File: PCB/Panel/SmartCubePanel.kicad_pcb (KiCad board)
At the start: 2 copper layers, 174.6 x 142.8 mm, 912 parts, among them J1 PogoPinPad, J1 SWD_Programmer, J1 Shield_Connector_Top_Left, J2 Conn_01x06, J2 Shield_Connector_Bottom_Left, J2 Shield_Connector_Top_Right, J3 PogoPinPad, J3 Shield_Connector_Bottom_Right, J3 Shield_Connector_Top_Right, J4 PogoPinPad, J4 Shield_Connector_Bottom_Right, J4 Shield_Connector_Top_Left, J5 Shield_Connector_Bottom_Left, U1 HallLinearSensor, U1 PY32F002BF15P6TU, U1 PogoPin, U2 PinHeaderTop, U2 PogoPin, U3 PinHeaderRight, U3 PogoPin, U4 PinHeaderBottom, U5 PinHeaderLeft

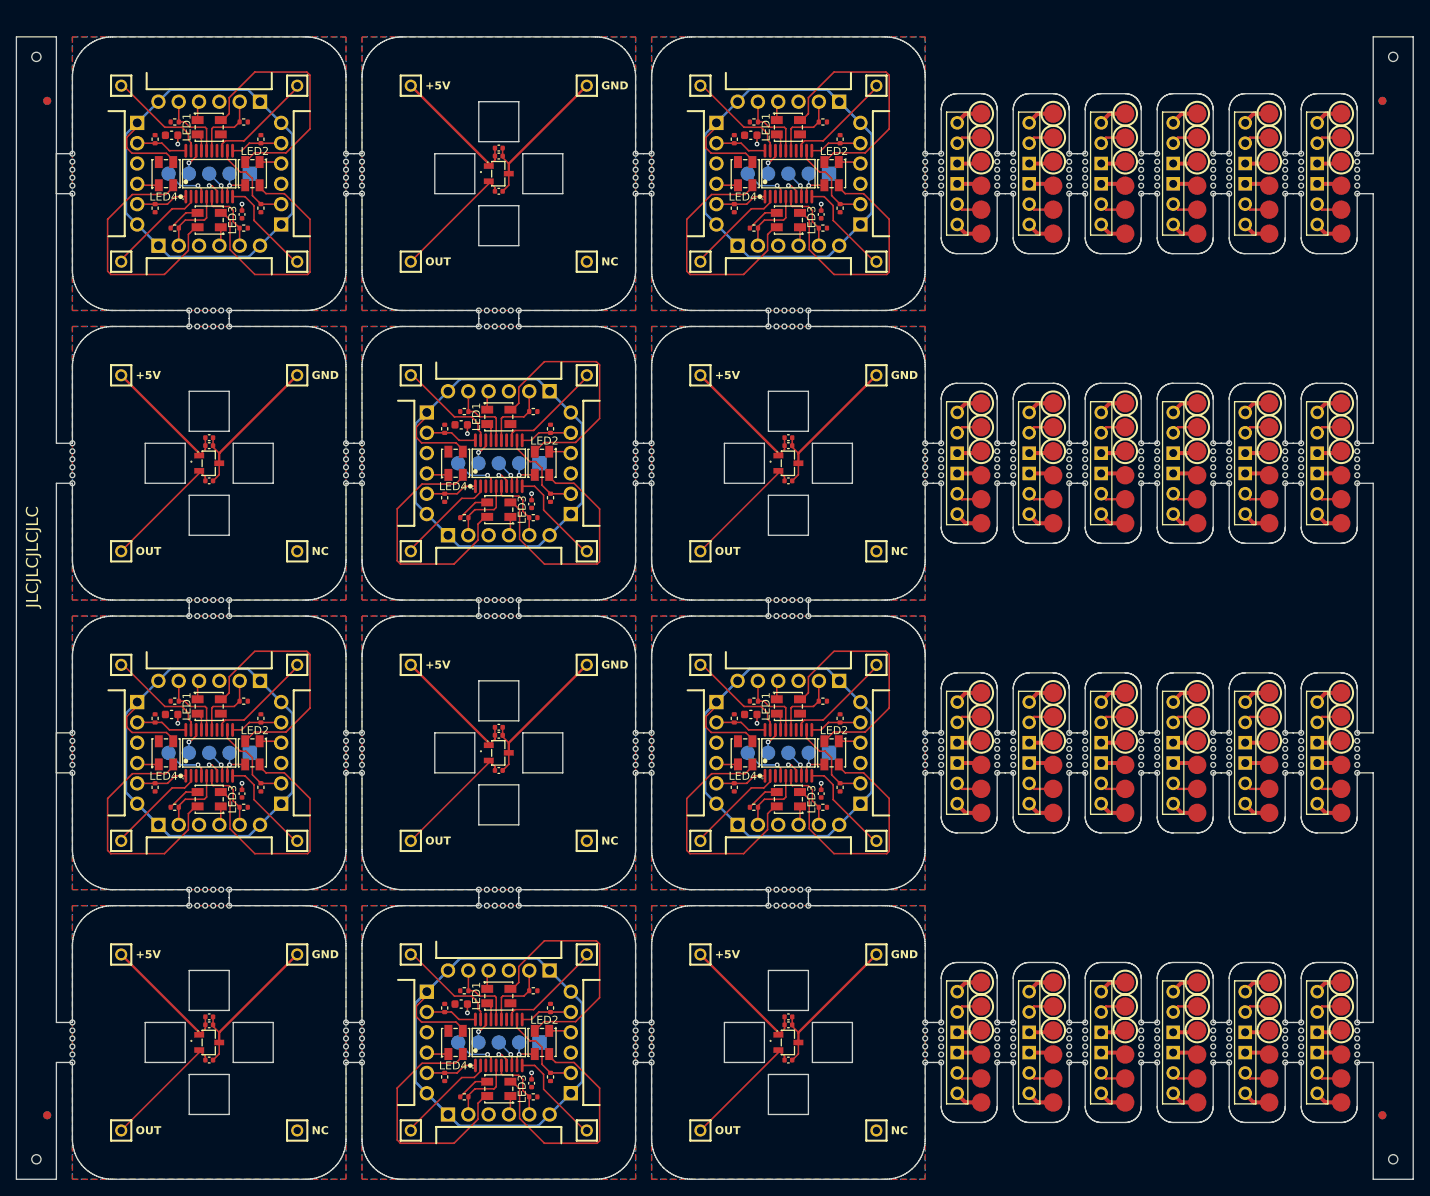
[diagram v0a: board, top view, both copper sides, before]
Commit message: Fix 3d model paths
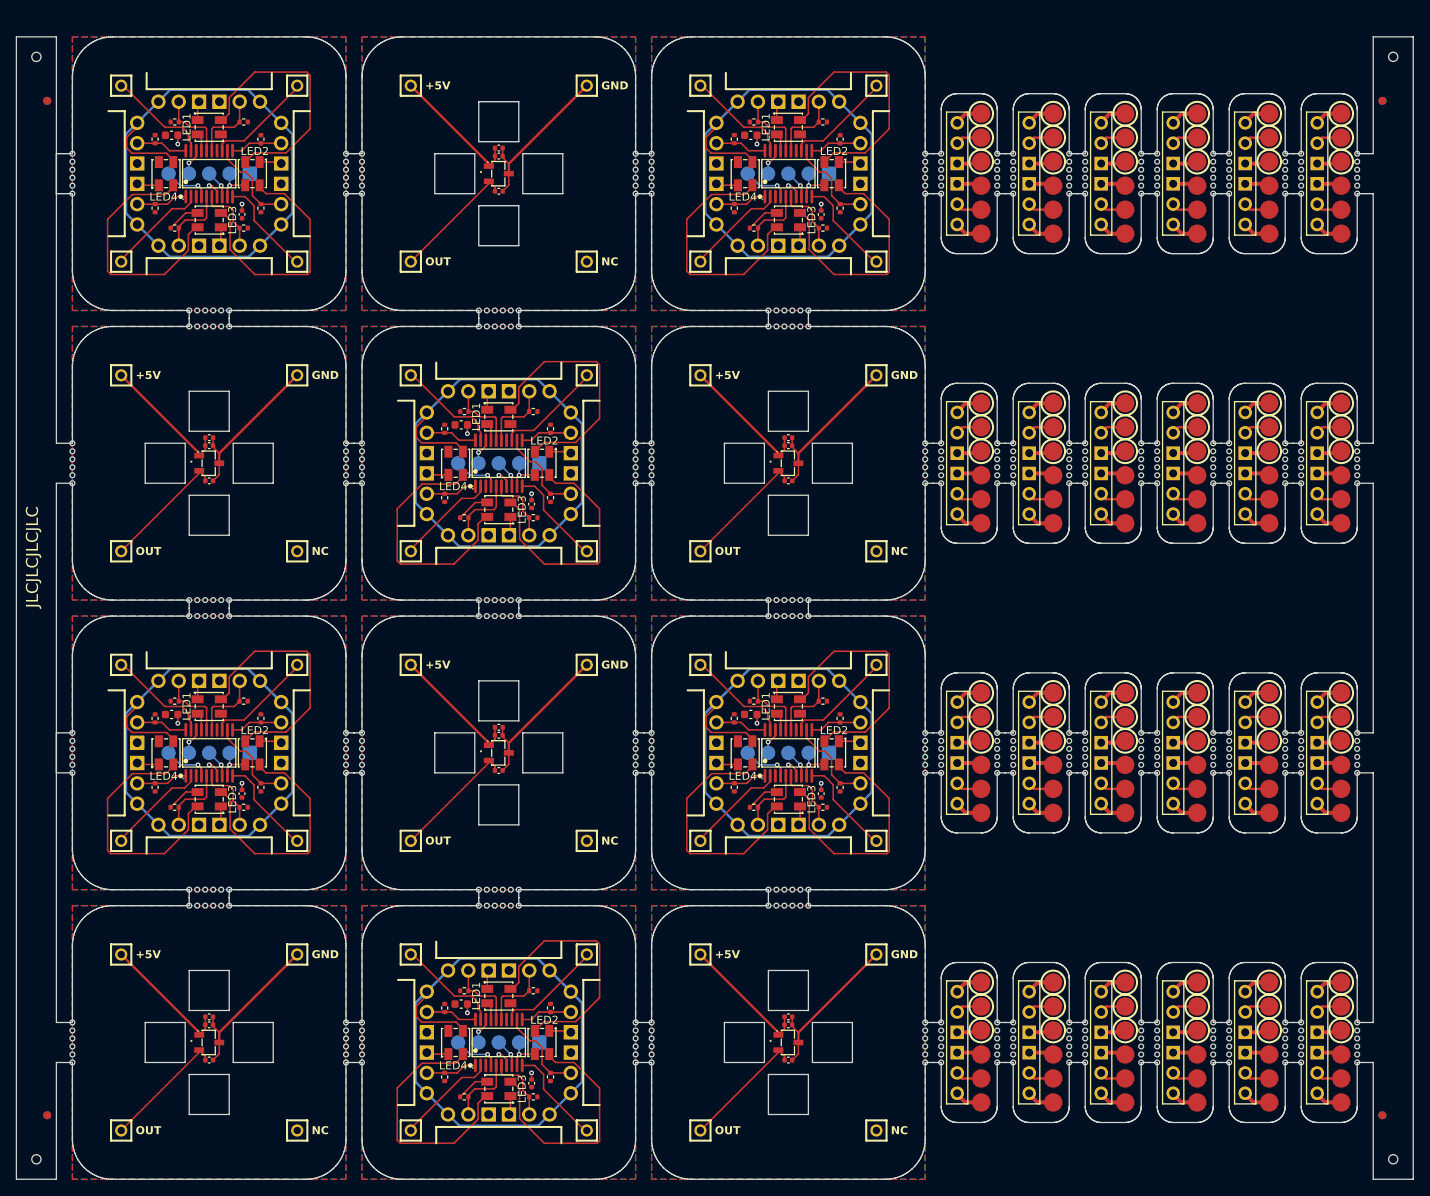
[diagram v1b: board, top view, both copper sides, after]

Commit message: Add power supply (wip) and update panel
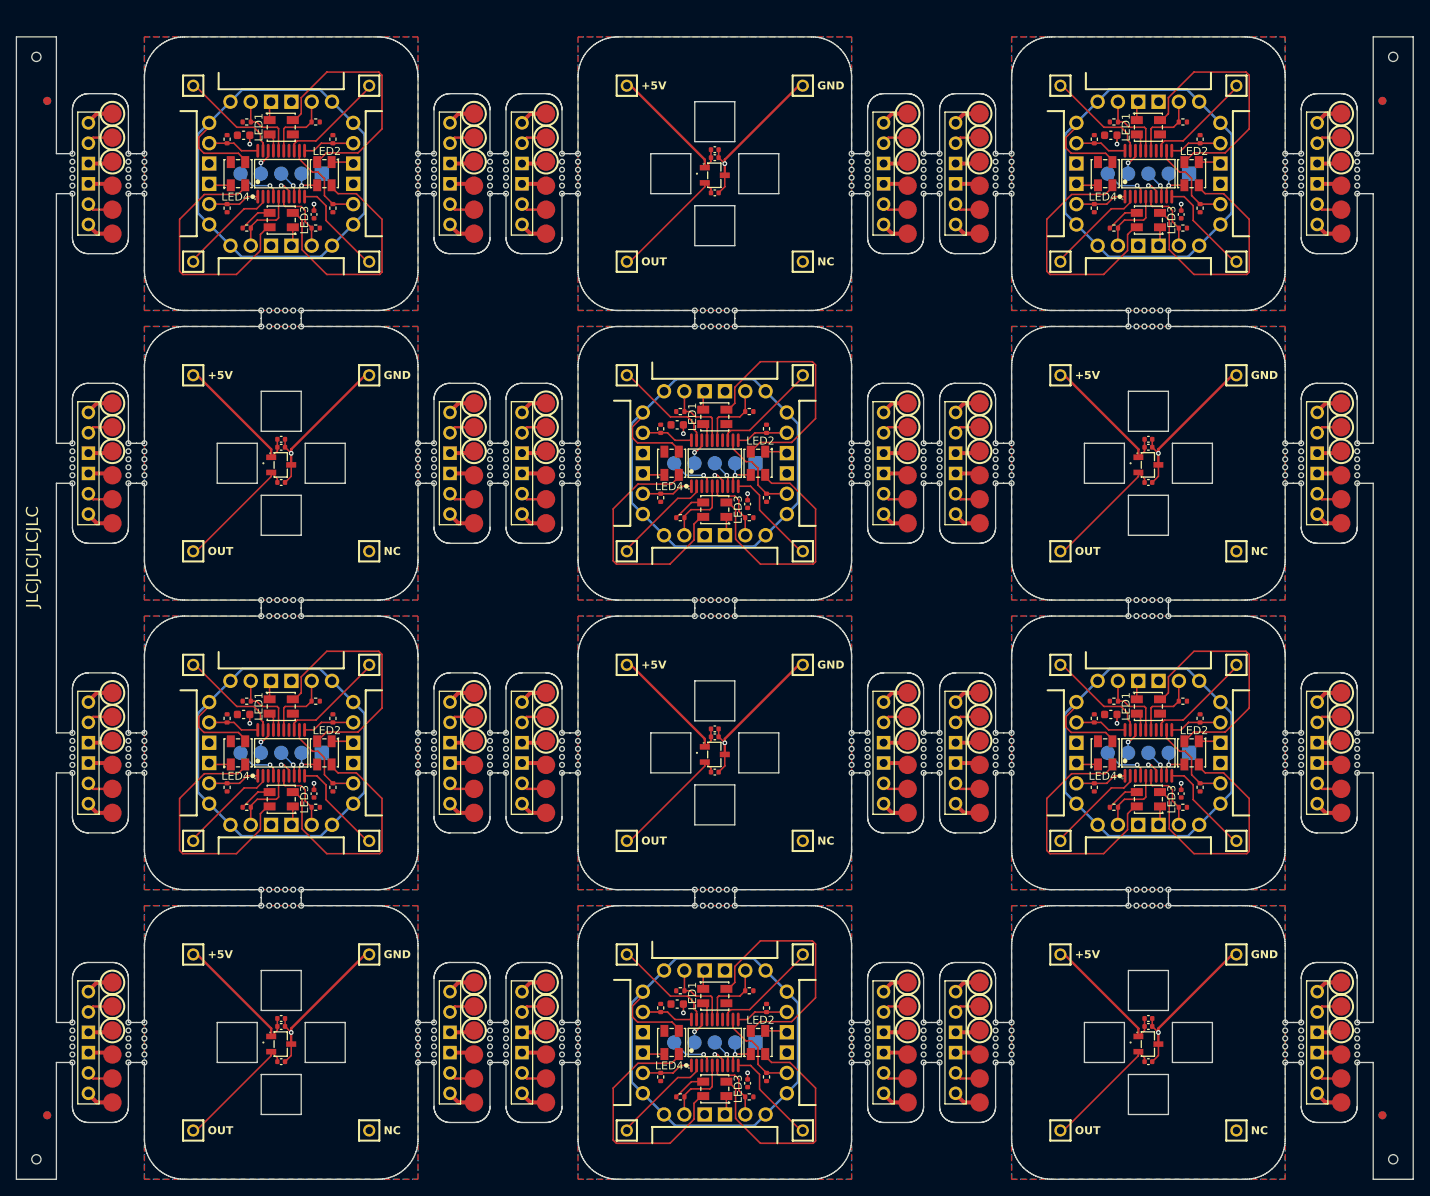
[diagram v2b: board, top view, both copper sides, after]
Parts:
- removed the C1 at (116.8, 68.5)
- removed the C1 at (153.0, 104.7)
- removed the C1 at (157.7, 147.9)
- removed the C1 at (85.3, 147.9)
- removed the C1 at (80.6, 32.3)
- removed the C1 at (153.0, 32.3)
- removed the C1 at (116.8, 140.9)
- removed the C1 at (85.3, 75.5)
- removed the C1 at (121.5, 111.7)
- removed the C1 at (157.7, 75.5)
- removed the C1 at (80.6, 104.7)
- removed the C1 at (121.5, 39.3)
- removed the C2 at (157.7, 70.1)
- removed the C2 at (85.3, 70.1)
- removed the C2 at (161.8, 114.6)
- removed the C2 at (161.8, 42.2)
- removed the C2 at (125.6, 78.4)
- removed the C2 at (89.4, 114.6)
- removed the C2 at (85.3, 142.5)
- removed the C2 at (125.6, 150.8)
- removed the C2 at (157.7, 142.5)
- removed the C2 at (121.5, 106.3)
- removed the C2 at (89.4, 42.2)
- removed the C2 at (121.5, 33.9)
- removed the C3 at (121.5, 34.9)
- removed the C3 at (85.3, 143.5)
- removed the C3 at (157.7, 143.5)
- removed the C3 at (157.7, 71.1)
- removed the C3 at (121.5, 107.3)
- removed the C3 at (85.3, 71.1)
- removed the J1 at (217.8, 38.6)
- removed the J1 at (217.8, 74.8)
- removed the J1 at (226.8, 147.2)
- removed the J1 at (181.8, 111.0)
- removed the J1 at (181.8, 74.8)
- removed the J1 at (217.8, 147.2)
- removed the J1 at (190.8, 111.0)
- removed the J1 at (199.8, 74.8)
- removed the J1 at (110.5, 26.1)
- removed the J1 at (181.8, 38.6)
- removed the J1 at (190.8, 38.6)
- removed the J1 at (146.7, 62.3)
- removed the J1 at (226.8, 74.8)
- removed the J1 at (217.8, 111.0)
- removed the J1 at (181.8, 147.2)
- removed the J1 at (146.7, 134.7)
- removed the J1 at (208.8, 111.0)
- removed the J1 at (208.8, 38.6)
- removed the J1 at (226.8, 38.6)
- removed the J1 at (74.3, 62.3)
- removed the J1 at (226.8, 111.0)
- removed the J1 at (208.8, 147.2)
- removed the J1 at (74.3, 134.7)
- removed the J1 at (199.8, 147.2)
- removed the J1 at (85.4, 109.5)
- removed the J1 at (157.8, 109.5)
- removed the J1 at (121.6, 73.3)
- removed the J1 at (157.8, 37.1)
- removed the J1 at (85.4, 37.1)
- removed the J1 at (121.6, 145.7)
- removed the J1 at (110.5, 98.5)
- removed the J1 at (190.8, 74.8)
- removed the J1 at (199.8, 38.6)
- removed the J1 at (190.8, 147.2)
- removed the J1 at (208.8, 74.8)
- removed the J1 at (199.8, 111.0)
- removed the J2 at (205.8, 37.1)
- removed the J2 at (132.5, 134.7)
- removed the J2 at (132.5, 62.3)
- removed the J2 at (74.3, 84.3)
- removed the J2 at (187.8, 145.7)
- removed the J2 at (205.8, 73.3)
- removed the J2 at (178.8, 145.7)
- removed the J2 at (110.5, 120.5)
- removed the J2 at (187.8, 37.1)
- removed the J2 at (214.8, 145.7)
- removed the J2 at (146.7, 156.7)
- removed the J2 at (110.5, 48.1)
- removed the J2 at (223.8, 37.1)
- removed the J2 at (196.8, 37.1)
- removed the J2 at (187.8, 109.5)
- removed the J2 at (178.8, 109.5)
- removed the J2 at (168.7, 26.1)
- removed the J2 at (146.7, 84.3)
- removed the J2 at (223.8, 73.3)
- removed the J2 at (214.8, 109.5)
- removed the J2 at (205.8, 109.5)
- removed the J2 at (178.8, 73.3)
- removed the J2 at (74.3, 156.7)
- removed the J2 at (96.3, 26.1)
- removed the J2 at (214.8, 37.1)
- removed the J2 at (187.8, 73.3)
- removed the J2 at (96.3, 98.5)
- removed the J2 at (223.8, 145.7)
- removed the J2 at (214.8, 73.3)
- removed the J2 at (196.8, 109.5)
- removed the J2 at (178.8, 37.1)
- removed the J2 at (168.7, 98.5)
- removed the J2 at (196.8, 73.3)
- removed the J2 at (205.8, 145.7)
- removed the J2 at (196.8, 145.7)
- removed the J2 at (223.8, 109.5)
- removed the J3 at (132.5, 26.1)
- removed the J3 at (208.8, 77.8)
- removed the J3 at (132.5, 84.3)
- removed the J3 at (208.8, 114.0)
- removed the J3 at (199.8, 150.2)
- removed the J3 at (132.5, 156.7)
- removed the J3 at (132.5, 98.5)
- removed the J3 at (96.3, 134.7)
- removed the J3 at (217.8, 150.2)
- removed the J3 at (226.8, 77.8)
- removed the J3 at (199.8, 114.0)
- removed the J3 at (190.8, 114.0)
- removed the J3 at (168.7, 62.3)
- removed the J3 at (226.8, 114.0)
- removed the J3 at (96.3, 62.3)
- removed the J3 at (181.8, 150.2)
- removed the J3 at (181.8, 77.8)
- removed the J3 at (199.8, 41.6)
- removed the J3 at (190.8, 77.8)
- removed the J3 at (96.3, 48.1)
- removed the J3 at (217.8, 41.6)
- removed the J3 at (168.7, 134.7)
- removed the J3 at (217.8, 77.8)
- removed the J3 at (181.8, 41.6)
- removed the J3 at (208.8, 150.2)
- removed the J3 at (190.8, 41.6)
- removed the J3 at (226.8, 150.2)
- removed the J3 at (168.7, 48.1)
- removed the J3 at (168.7, 120.5)
- removed the J3 at (96.3, 120.5)
- removed the J3 at (181.8, 114.0)
- removed the J3 at (208.8, 41.6)
- removed the J3 at (226.8, 41.6)
- removed the J3 at (217.8, 114.0)
- removed the J3 at (199.8, 77.8)
- removed the J3 at (190.8, 150.2)
- removed the J4 at (208.8, 117.0)
- removed the J4 at (146.7, 26.1)
- removed the J4 at (181.8, 44.6)
- removed the J4 at (168.7, 156.7)
- removed the J4 at (181.8, 117.0)
- removed the J4 at (217.8, 153.2)
- removed the J4 at (190.8, 80.8)
- removed the J4 at (132.5, 120.5)
- removed the J4 at (208.8, 44.6)
- removed the J4 at (208.8, 153.2)
- removed the J4 at (96.3, 84.3)
- removed the J4 at (74.3, 98.5)
- removed the J4 at (226.8, 117.0)
- removed the J4 at (181.8, 153.2)
- removed the J4 at (132.5, 48.1)
- removed the J4 at (217.8, 44.6)
- removed the J4 at (226.8, 80.8)
- removed the J4 at (199.8, 44.6)
- removed the J4 at (74.3, 26.1)
- removed the J4 at (199.8, 117.0)
- removed the J4 at (199.8, 153.2)
- removed the J4 at (110.5, 134.7)
- removed the J4 at (226.8, 44.6)
- removed the J4 at (168.7, 84.3)
- removed the J4 at (208.8, 80.8)
- removed the J4 at (226.8, 153.2)
- removed the J4 at (190.8, 44.6)
- removed the J4 at (181.8, 80.8)
- removed the J4 at (190.8, 117.0)
- removed the J4 at (190.8, 153.2)
- removed the J4 at (217.8, 117.0)
- removed the J4 at (96.3, 156.7)
- removed the J4 at (110.5, 62.3)
- removed the J4 at (199.8, 80.8)
- removed the J4 at (217.8, 80.8)
- removed the J4 at (146.7, 98.5)
- removed the J5 at (146.7, 48.1)
- removed the J5 at (74.3, 48.1)
- removed the J5 at (110.5, 156.7)
- removed the J5 at (74.3, 120.5)
- removed the J5 at (146.7, 120.5)
- removed the J5 at (110.5, 84.3)
- removed the LED1 at (157.7, 103.7)
- removed the LED1 at (121.5, 67.5)
- removed the LED1 at (85.3, 31.3)
- removed the LED1 at (85.3, 103.7)
- removed the LED1 at (157.7, 31.3)
- removed the LED1 at (121.5, 139.9)
- removed the LED2 at (163.1, 109.5)
- removed the LED2 at (163.1, 37.1)
- removed the LED2 at (126.9, 73.3)
- removed the LED2 at (90.7, 109.5)
- removed the LED2 at (90.7, 37.1)
- removed the LED2 at (126.9, 145.7)
- removed the LED3 at (85.3, 115.3)
- removed the LED3 at (85.3, 42.9)
- removed the LED3 at (157.7, 42.9)
- removed the LED3 at (157.7, 115.3)
- removed the LED3 at (121.5, 79.1)
- removed the LED3 at (121.5, 151.5)
- removed the LED4 at (116.1, 73.3)
- removed the LED4 at (79.9, 109.5)
- removed the LED4 at (152.3, 37.1)
- removed the LED4 at (116.1, 145.7)
- removed the LED4 at (152.3, 109.5)
- removed the LED4 at (79.9, 37.1)
- removed the R1 at (117.2, 66.8)
- removed the R1 at (117.2, 139.2)
- removed the R1 at (153.4, 30.6)
- removed the R1 at (81.0, 103.0)
- removed the R1 at (81.0, 30.6)
- removed the R1 at (153.4, 103.0)
- removed the R2 at (89.6, 103.0)
- removed the R2 at (125.8, 66.8)
- removed the R2 at (162.0, 103.0)
- removed the R2 at (125.8, 139.2)
- removed the R2 at (89.6, 30.6)
- removed the R2 at (162.0, 30.6)
- removed the R3 at (91.8, 105.2)
- removed the R3 at (164.2, 32.8)
- removed the R3 at (128.0, 141.4)
- removed the R3 at (128.0, 69.0)
- removed the R3 at (164.2, 105.2)
- removed the R3 at (91.8, 32.8)
- removed the R4 at (164.2, 113.8)
- removed the R4 at (91.8, 41.4)
- removed the R4 at (128.0, 77.6)
- removed the R4 at (91.8, 113.8)
- removed the R4 at (128.0, 150.0)
- removed the R4 at (164.2, 41.4)
- removed the R5 at (125.8, 152.5)
- removed the R5 at (125.8, 80.1)
- removed the R5 at (89.6, 43.9)
- removed the R5 at (162.0, 43.9)
- removed the R5 at (89.6, 116.3)
- removed the R5 at (162.0, 116.3)
- removed the R6 at (81.0, 116.3)
- removed the R6 at (117.2, 152.5)
- removed the R6 at (153.4, 43.9)
- removed the R6 at (153.4, 116.3)
- removed the R6 at (81.0, 43.9)
- removed the R6 at (117.2, 80.1)
- removed the R7 at (78.5, 113.8)
- removed the R7 at (78.5, 41.4)
- removed the R7 at (150.9, 113.8)
- removed the R7 at (150.9, 41.4)
- removed the R7 at (114.7, 150.0)
- removed the R7 at (114.7, 77.6)
- removed the R8 at (114.7, 141.4)
- removed the R8 at (78.5, 105.2)
- removed the R8 at (114.7, 69.0)
- removed the R8 at (78.5, 32.8)
- removed the R8 at (150.9, 105.2)
- removed the R8 at (150.9, 32.8)
- removed the U1 at (181.8, 102.0)
- removed the U1 at (190.8, 65.8)
- removed the U1 at (226.8, 102.0)
- removed the U1 at (226.8, 65.8)
- removed the U1 at (181.8, 29.6)
- removed the U1 at (121.5, 37.1)
- removed the U1 at (190.8, 29.6)
- removed the U1 at (190.8, 102.0)
- removed the U1 at (121.5, 109.5)
- removed the U1 at (199.8, 65.8)
- removed the U1 at (157.7, 145.7)
- removed the U1 at (208.8, 138.2)
- removed the U1 at (217.8, 138.2)
- removed the U1 at (121.5, 73.3)
- removed the U1 at (121.5, 145.7)
- removed the U1 at (157.7, 109.5)
- removed the U1 at (181.8, 65.8)
- removed the U1 at (157.7, 37.1)
- removed the U1 at (85.3, 73.3)
- removed the U1 at (208.8, 29.6)
- removed the U1 at (217.8, 29.6)
- removed the U1 at (199.8, 29.6)
- removed the U1 at (208.8, 102.0)
- removed the U1 at (190.8, 138.2)
- removed the U1 at (85.3, 37.1)
- removed the U1 at (85.3, 109.5)
- removed the U1 at (199.8, 138.2)
- removed the U1 at (181.8, 138.2)
- removed the U1 at (199.8, 102.0)
- removed the U1 at (217.8, 102.0)
- removed the U1 at (157.7, 73.3)
- removed the U1 at (208.8, 65.8)
- removed the U1 at (85.3, 145.7)
- removed the U1 at (226.8, 138.2)
- removed the U1 at (217.8, 65.8)
- removed the U1 at (226.8, 29.6)
- removed the U2 at (181.8, 141.2)
- removed the U2 at (190.8, 105.0)
- removed the U2 at (190.8, 141.2)
- removed the U2 at (226.8, 68.8)
- removed the U2 at (181.8, 32.6)
- removed the U2 at (217.8, 105.0)
- removed the U2 at (157.7, 28.1)
- removed the U2 at (199.8, 68.8)
- removed the U2 at (217.8, 141.2)
- removed the U2 at (190.8, 68.8)
- removed the U2 at (199.8, 141.2)
- removed the U2 at (226.8, 105.0)
- removed the U2 at (226.8, 141.2)
- removed the U2 at (121.5, 136.7)
- removed the U2 at (85.3, 28.1)
- removed the U2 at (157.7, 100.5)
- removed the U2 at (121.5, 64.3)
- removed the U2 at (208.8, 32.6)
- removed the U2 at (226.8, 32.6)
- removed the U2 at (181.8, 105.0)
- removed the U2 at (208.8, 141.2)
- removed the U2 at (217.8, 32.6)
- removed the U2 at (181.8, 68.8)
- removed the U2 at (199.8, 105.0)
- removed the U2 at (199.8, 32.6)
- removed the U2 at (208.8, 105.0)
- removed the U2 at (85.3, 100.5)
- removed the U2 at (190.8, 32.6)
- removed the U2 at (217.8, 68.8)
- removed the U2 at (208.8, 68.8)
- removed the U3 at (208.8, 71.8)
- removed the U3 at (199.8, 144.2)
- removed the U3 at (199.8, 71.8)
- removed the U3 at (226.8, 108.0)
- removed the U3 at (226.8, 35.6)
- removed the U3 at (166.7, 109.5)
- removed the U3 at (190.8, 71.8)
- removed the U3 at (217.8, 108.0)
- removed the U3 at (208.8, 144.2)
- removed the U3 at (181.8, 71.8)
- removed the U3 at (199.8, 35.6)
- removed the U3 at (94.3, 37.1)
- removed the U3 at (217.8, 35.6)
- removed the U3 at (217.8, 71.8)
- removed the U3 at (190.8, 144.2)
- removed the U3 at (181.8, 144.2)
- removed the U3 at (181.8, 108.0)
- removed the U3 at (208.8, 108.0)
- removed the U3 at (226.8, 144.2)
- removed the U3 at (181.8, 35.6)
- removed the U3 at (190.8, 108.0)
- removed the U3 at (217.8, 144.2)
- removed the U3 at (94.3, 109.5)
- removed the U3 at (130.5, 73.3)
- removed the U3 at (190.8, 35.6)
- removed the U3 at (130.5, 145.7)
- removed the U3 at (199.8, 108.0)
- removed the U3 at (208.8, 35.6)
- removed the U3 at (226.8, 71.8)
- removed the U3 at (166.7, 37.1)
- removed the U4 at (121.5, 154.7)
- removed the U4 at (85.3, 46.1)
- removed the U4 at (85.3, 118.5)
- removed the U4 at (157.7, 118.5)
- removed the U4 at (121.5, 82.3)
- removed the U4 at (157.7, 46.1)
- removed the U5 at (112.5, 145.7)
- removed the U5 at (148.7, 37.1)
- removed the U5 at (148.7, 109.5)
- removed the U5 at (76.3, 37.1)
- removed the U5 at (76.3, 109.5)
- removed the U5 at (112.5, 73.3)
- added C1: 10nF, Capacitor_SMD:C_0402_1005Metric, F.Cu at (94.3, 148.1)
- added C1: 10uF, Capacitor_SMD:C_0603_1608Metric, F.Cu at (198.0, 104.7)
- added C1: 10uF, Capacitor_SMD:C_0603_1608Metric, F.Cu at (89.6, 104.7)
- added C1: 10nF, Capacitor_SMD:C_0402_1005Metric, F.Cu at (202.7, 148.1)
- added C1: 10nF, Capacitor_SMD:C_0402_1005Metric, F.Cu at (94.3, 75.7)
- added C1: 10uF, Capacitor_SMD:C_0603_1608Metric, F.Cu at (143.8, 140.9)
- added C1: 10uF, Capacitor_SMD:C_0603_1608Metric, F.Cu at (143.8, 68.5)
- added C1: 10uF, Capacitor_SMD:C_0603_1608Metric, F.Cu at (89.6, 32.3)
- added C1: 10uF, Capacitor_SMD:C_0603_1608Metric, F.Cu at (198.0, 32.3)
- added C1: 10nF, Capacitor_SMD:C_0402_1005Metric, F.Cu at (148.5, 39.5)
- added C1: 10nF, Capacitor_SMD:C_0402_1005Metric, F.Cu at (148.5, 111.9)
- added C1: 10nF, Capacitor_SMD:C_0402_1005Metric, F.Cu at (202.7, 75.7)
- added C2: 1nF, Capacitor_SMD:C_0402_1005Metric, F.Cu at (202.7, 70.3)
- added C2: 1nF, Capacitor_SMD:C_0402_1005Metric, F.Cu at (94.3, 142.7)
- added C2: 100nF, Capacitor_SMD:C_0402_1005Metric, F.Cu at (206.8, 114.6)
- added C2: 100nF, Capacitor_SMD:C_0402_1005Metric, F.Cu at (98.4, 42.2)
- added C2: 1nF, Capacitor_SMD:C_0402_1005Metric, F.Cu at (148.5, 34.1)
- added C2: 1nF, Capacitor_SMD:C_0402_1005Metric, F.Cu at (202.7, 142.7)
- added C2: 100nF, Capacitor_SMD:C_0402_1005Metric, F.Cu at (152.6, 150.8)
- added C2: 100nF, Capacitor_SMD:C_0402_1005Metric, F.Cu at (206.8, 42.2)
- added C2: 1nF, Capacitor_SMD:C_0402_1005Metric, F.Cu at (94.3, 70.3)
- added C2: 1nF, Capacitor_SMD:C_0402_1005Metric, F.Cu at (148.5, 106.5)
- added C2: 100nF, Capacitor_SMD:C_0402_1005Metric, F.Cu at (98.4, 114.6)
- added C2: 100nF, Capacitor_SMD:C_0402_1005Metric, F.Cu at (152.6, 78.4)
- added C3: 1nF, Capacitor_SMD:C_0402_1005Metric, F.Cu at (148.5, 35.1)
- added C3: 1nF, Capacitor_SMD:C_0402_1005Metric, F.Cu at (202.7, 71.3)
- added C3: 1nF, Capacitor_SMD:C_0402_1005Metric, F.Cu at (202.7, 143.7)
- added C3: 1nF, Capacitor_SMD:C_0402_1005Metric, F.Cu at (94.3, 71.3)
- added C3: 1nF, Capacitor_SMD:C_0402_1005Metric, F.Cu at (94.3, 143.7)
- added C3: 1nF, Capacitor_SMD:C_0402_1005Metric, F.Cu at (148.5, 107.5)
- added J1: PogoPinPad, CustomFootprints:PogoPinPad, F.Cu at (118.4, 38.6)
- added J1: PogoPinPad, CustomFootprints:PogoPinPad, F.Cu at (181.6, 74.8)
- added J1: PogoPinPad, CustomFootprints:PogoPinPad, F.Cu at (181.6, 111.0)
- added J1: PogoPinPad, CustomFootprints:PogoPinPad, F.Cu at (73.2, 147.2)
- added J1: Shield_Connector_Top_Left, CustomFootprints:HDR-TH_1P-V-F-1, F.Cu at (83.3, 62.3)
- added J1: PogoPinPad, CustomFootprints:PogoPinPad, F.Cu at (118.4, 111.0)
- added J1: Shield_Connector_Top_Left, CustomFootprints:HDR-TH_1P-V-F-1, F.Cu at (83.3, 134.7)
- added J1: PogoPinPad, CustomFootprints:PogoPinPad, F.Cu at (226.8, 111.0)
- added J1: PogoPinPad, CustomFootprints:PogoPinPad, F.Cu at (172.6, 74.8)
- added J1: PogoPinPad, CustomFootprints:PogoPinPad, F.Cu at (226.8, 38.6)
- added J1: PogoPinPad, CustomFootprints:PogoPinPad, F.Cu at (73.2, 38.6)
- added J1: PogoPinPad, CustomFootprints:PogoPinPad, F.Cu at (181.6, 38.6)
- added J1: PogoPinPad, CustomFootprints:PogoPinPad, F.Cu at (172.6, 38.6)
- added J1: Shield_Connector_Top_Left, CustomFootprints:HDR-TH_1P-V-F-1, F.Cu at (137.5, 98.5)
- added J1: PogoPinPad, CustomFootprints:PogoPinPad, F.Cu at (172.6, 111.0)
- added J1: PogoPinPad, CustomFootprints:PogoPinPad, F.Cu at (127.4, 147.2)
- added J1: PogoPinPad, CustomFootprints:PogoPinPad, F.Cu at (73.2, 74.8)
- added J1: Shield_Connector_Top_Left, CustomFootprints:HDR-TH_1P-V-F-1, F.Cu at (191.7, 134.7)
- added J1: PogoPinPad, CustomFootprints:PogoPinPad, F.Cu at (118.4, 147.2)
- added J1: PogoPinPad, CustomFootprints:PogoPinPad, F.Cu at (73.2, 111.0)
- added J1: PogoPinPad, CustomFootprints:PogoPinPad, F.Cu at (127.4, 111.0)
- added J1: PogoPinPad, CustomFootprints:PogoPinPad, F.Cu at (226.8, 147.2)
- added J1: PogoPinPad, CustomFootprints:PogoPinPad, F.Cu at (226.8, 74.8)
- added J1: PogoPinPad, CustomFootprints:PogoPinPad, F.Cu at (118.4, 74.8)
- added J1: SWD_Programmer, CustomFootprints:SWD_Pad, B.Cu at (94.4, 109.5)
- added J1: SWD_Programmer, CustomFootprints:SWD_Pad, B.Cu at (94.4, 37.1)
- added J1: SWD_Programmer, CustomFootprints:SWD_Pad, B.Cu at (148.6, 145.7)
- added J1: SWD_Programmer, CustomFootprints:SWD_Pad, B.Cu at (202.8, 109.5)
- added J1: SWD_Programmer, CustomFootprints:SWD_Pad, B.Cu at (148.6, 73.3)
- added J1: SWD_Programmer, CustomFootprints:SWD_Pad, B.Cu at (202.8, 37.1)
- added J1: PogoPinPad, CustomFootprints:PogoPinPad, F.Cu at (127.4, 38.6)
- added J1: PogoPinPad, CustomFootprints:PogoPinPad, F.Cu at (127.4, 74.8)
- added J1: PogoPinPad, CustomFootprints:PogoPinPad, F.Cu at (172.6, 147.2)
- added J1: PogoPinPad, CustomFootprints:PogoPinPad, F.Cu at (181.6, 147.2)
- added J1: Shield_Connector_Top_Left, CustomFootprints:HDR-TH_1P-V-F-1, F.Cu at (191.7, 62.3)
- added J1: Shield_Connector_Top_Left, CustomFootprints:HDR-TH_1P-V-F-1, F.Cu at (137.5, 26.1)
- added J2: Conn_01x06, CustomFootprints:Connector_PinHeader_2.54mm_Vertical, F.Cu at (115.4, 73.3)
- added J2: Conn_01x06, CustomFootprints:Connector_PinHeader_2.54mm_Vertical, F.Cu at (115.4, 37.1)
- added J2: Conn_01x06, CustomFootprints:Connector_PinHeader_2.54mm_Vertical, F.Cu at (178.6, 73.3)
- added J2: Conn_01x06, CustomFootprints:Connector_PinHeader_2.54mm_Vertical, F.Cu at (70.2, 73.3)
- added J2: Conn_01x06, CustomFootprints:Connector_PinHeader_2.54mm_Vertical, F.Cu at (124.4, 73.3)
- added J2: Conn_01x06, CustomFootprints:Connector_PinHeader_2.54mm_Vertical, F.Cu at (70.2, 109.5)
- added J2: Conn_01x06, CustomFootprints:Connector_PinHeader_2.54mm_Vertical, F.Cu at (169.6, 109.5)
- added J2: Shield_Connector_Bottom_Left, CustomFootprints:HDR-TH_1P-V-F-1, F.Cu at (137.5, 120.5)
- added J2: Shield_Connector_Bottom_Left, CustomFootprints:HDR-TH_1P-V-F-1, F.Cu at (83.3, 156.7)
- added J2: Conn_01x06, CustomFootprints:Connector_PinHeader_2.54mm_Vertical, F.Cu at (169.6, 37.1)
- added J2: Conn_01x06, CustomFootprints:Connector_PinHeader_2.54mm_Vertical, F.Cu at (223.8, 37.1)
- added J2: Shield_Connector_Top_Right, CustomFootprints:HDR-TH_1P-V-F-1, F.Cu at (105.3, 98.5)
- added J2: Shield_Connector_Bottom_Left, CustomFootprints:HDR-TH_1P-V-F-1, F.Cu at (137.5, 48.1)
- added J2: Conn_01x06, CustomFootprints:Connector_PinHeader_2.54mm_Vertical, F.Cu at (178.6, 145.7)
- added J2: Conn_01x06, CustomFootprints:Connector_PinHeader_2.54mm_Vertical, F.Cu at (169.6, 73.3)
- added J2: Shield_Connector_Top_Right, CustomFootprints:HDR-TH_1P-V-F-1, F.Cu at (159.5, 134.7)
- added J2: Conn_01x06, CustomFootprints:Connector_PinHeader_2.54mm_Vertical, F.Cu at (115.4, 145.7)
- added J2: Conn_01x06, CustomFootprints:Connector_PinHeader_2.54mm_Vertical, F.Cu at (124.4, 109.5)
- added J2: Shield_Connector_Bottom_Left, CustomFootprints:HDR-TH_1P-V-F-1, F.Cu at (191.7, 84.3)
- added J2: Shield_Connector_Top_Right, CustomFootprints:HDR-TH_1P-V-F-1, F.Cu at (213.7, 98.5)
- added J2: Conn_01x06, CustomFootprints:Connector_PinHeader_2.54mm_Vertical, F.Cu at (223.8, 109.5)
- added J2: Conn_01x06, CustomFootprints:Connector_PinHeader_2.54mm_Vertical, F.Cu at (70.2, 37.1)
- added J2: Shield_Connector_Bottom_Left, CustomFootprints:HDR-TH_1P-V-F-1, F.Cu at (83.3, 84.3)
- added J2: Shield_Connector_Bottom_Left, CustomFootprints:HDR-TH_1P-V-F-1, F.Cu at (191.7, 156.7)
- added J2: Conn_01x06, CustomFootprints:Connector_PinHeader_2.54mm_Vertical, F.Cu at (124.4, 145.7)
- added J2: Shield_Connector_Top_Right, CustomFootprints:HDR-TH_1P-V-F-1, F.Cu at (159.5, 62.3)
- added J2: Shield_Connector_Top_Right, CustomFootprints:HDR-TH_1P-V-F-1, F.Cu at (105.3, 26.1)
- added J2: Conn_01x06, CustomFootprints:Connector_PinHeader_2.54mm_Vertical, F.Cu at (115.4, 109.5)
- added J2: Shield_Connector_Top_Right, CustomFootprints:HDR-TH_1P-V-F-1, F.Cu at (213.7, 26.1)
- added J2: Conn_01x06, CustomFootprints:Connector_PinHeader_2.54mm_Vertical, F.Cu at (124.4, 37.1)
- added J2: Conn_01x06, CustomFootprints:Connector_PinHeader_2.54mm_Vertical, F.Cu at (223.8, 145.7)
- added J2: Conn_01x06, CustomFootprints:Connector_PinHeader_2.54mm_Vertical, F.Cu at (178.6, 37.1)
- added J2: Conn_01x06, CustomFootprints:Connector_PinHeader_2.54mm_Vertical, F.Cu at (169.6, 145.7)
- added J2: Conn_01x06, CustomFootprints:Connector_PinHeader_2.54mm_Vertical, F.Cu at (178.6, 109.5)
- added J2: Conn_01x06, CustomFootprints:Connector_PinHeader_2.54mm_Vertical, F.Cu at (70.2, 145.7)
- added J2: Conn_01x06, CustomFootprints:Connector_PinHeader_2.54mm_Vertical, F.Cu at (223.8, 73.3)
- added J3: PogoPinPad, CustomFootprints:PogoPinPad, F.Cu at (181.6, 77.8)
- added J3: PogoPinPad, CustomFootprints:PogoPinPad, F.Cu at (226.8, 41.6)
- added J3: PogoPinPad, CustomFootprints:PogoPinPad, F.Cu at (181.6, 114.0)
- added J3: PogoPinPad, CustomFootprints:PogoPinPad, F.Cu at (127.4, 114.0)
- added J3: PogoPinPad, CustomFootprints:PogoPinPad, F.Cu at (226.8, 77.8)
- added J3: PogoPinPad, CustomFootprints:PogoPinPad, F.Cu at (118.4, 114.0)
- added J3: PogoPinPad, CustomFootprints:PogoPinPad, F.Cu at (118.4, 41.6)
- added J3: PogoPinPad, CustomFootprints:PogoPinPad, F.Cu at (226.8, 150.2)
- added J3: PogoPinPad, CustomFootprints:PogoPinPad, F.Cu at (127.4, 150.2)
- added J3: PogoPinPad, CustomFootprints:PogoPinPad, F.Cu at (172.6, 150.2)
- added J3: PogoPinPad, CustomFootprints:PogoPinPad, F.Cu at (73.2, 114.0)
- added J3: Shield_Connector_Bottom_Right, CustomFootprints:HDR-TH_1P-V-F-1, F.Cu at (105.3, 48.1)
- added J3: PogoPinPad, CustomFootprints:PogoPinPad, F.Cu at (181.6, 150.2)
- added J3: Shield_Connector_Bottom_Right, CustomFootprints:HDR-TH_1P-V-F-1, F.Cu at (159.5, 156.7)
- added J3: Shield_Connector_Top_Right, CustomFootprints:HDR-TH_1P-V-F-1, F.Cu at (159.5, 26.1)
- added J3: PogoPinPad, CustomFootprints:PogoPinPad, F.Cu at (172.6, 114.0)
- added J3: Shield_Connector_Top_Right, CustomFootprints:HDR-TH_1P-V-F-1, F.Cu at (105.3, 62.3)
- added J3: PogoPinPad, CustomFootprints:PogoPinPad, F.Cu at (172.6, 77.8)
- added J3: PogoPinPad, CustomFootprints:PogoPinPad, F.Cu at (73.2, 150.2)
- added J3: PogoPinPad, CustomFootprints:PogoPinPad, F.Cu at (181.6, 41.6)
- added J3: PogoPinPad, CustomFootprints:PogoPinPad, F.Cu at (73.2, 41.6)
- added J3: PogoPinPad, CustomFootprints:PogoPinPad, F.Cu at (226.8, 114.0)
- added J3: PogoPinPad, CustomFootprints:PogoPinPad, F.Cu at (118.4, 150.2)
- added J3: Shield_Connector_Top_Right, CustomFootprints:HDR-TH_1P-V-F-1, F.Cu at (105.3, 134.7)
- added J3: PogoPinPad, CustomFootprints:PogoPinPad, F.Cu at (127.4, 77.8)
- added J3: PogoPinPad, CustomFootprints:PogoPinPad, F.Cu at (118.4, 77.8)
- added J3: Shield_Connector_Top_Right, CustomFootprints:HDR-TH_1P-V-F-1, F.Cu at (213.7, 62.3)
- added J3: PogoPinPad, CustomFootprints:PogoPinPad, F.Cu at (73.2, 77.8)
- added J3: Shield_Connector_Bottom_Right, CustomFootprints:HDR-TH_1P-V-F-1, F.Cu at (105.3, 120.5)
- added J3: Shield_Connector_Bottom_Right, CustomFootprints:HDR-TH_1P-V-F-1, F.Cu at (159.5, 84.3)
- added J3: Shield_Connector_Top_Right, CustomFootprints:HDR-TH_1P-V-F-1, F.Cu at (213.7, 134.7)
- added J3: Shield_Connector_Bottom_Right, CustomFootprints:HDR-TH_1P-V-F-1, F.Cu at (213.7, 48.1)
- added J3: PogoPinPad, CustomFootprints:PogoPinPad, F.Cu at (172.6, 41.6)
- added J3: Shield_Connector_Top_Right, CustomFootprints:HDR-TH_1P-V-F-1, F.Cu at (159.5, 98.5)
- added J3: PogoPinPad, CustomFootprints:PogoPinPad, F.Cu at (127.4, 41.6)
- added J3: Shield_Connector_Bottom_Right, CustomFootprints:HDR-TH_1P-V-F-1, F.Cu at (213.7, 120.5)
- added J4: PogoPinPad, CustomFootprints:PogoPinPad, F.Cu at (73.2, 80.8)
- added J4: PogoPinPad, CustomFootprints:PogoPinPad, F.Cu at (226.8, 153.2)
- added J4: PogoPinPad, CustomFootprints:PogoPinPad, F.Cu at (172.6, 153.2)
- added J4: PogoPinPad, CustomFootprints:PogoPinPad, F.Cu at (226.8, 80.8)
- added J4: PogoPinPad, CustomFootprints:PogoPinPad, F.Cu at (73.2, 117.0)
- added J4: Shield_Connector_Top_Left, CustomFootprints:HDR-TH_1P-V-F-1, F.Cu at (83.3, 98.5)
- added J4: Shield_Connector_Bottom_Right, CustomFootprints:HDR-TH_1P-V-F-1, F.Cu at (159.5, 120.5)
- added J4: Shield_Connector_Top_Left, CustomFootprints:HDR-TH_1P-V-F-1, F.Cu at (137.5, 62.3)
- added J4: PogoPinPad, CustomFootprints:PogoPinPad, F.Cu at (127.4, 44.6)
- added J4: PogoPinPad, CustomFootprints:PogoPinPad, F.Cu at (118.4, 80.8)
- added J4: PogoPinPad, CustomFootprints:PogoPinPad, F.Cu at (181.6, 153.2)
- added J4: PogoPinPad, CustomFootprints:PogoPinPad, F.Cu at (172.6, 44.6)
- added J4: PogoPinPad, CustomFootprints:PogoPinPad, F.Cu at (118.4, 153.2)
- added J4: PogoPinPad, CustomFootprints:PogoPinPad, F.Cu at (172.6, 117.0)
- added J4: Shield_Connector_Top_Left, CustomFootprints:HDR-TH_1P-V-F-1, F.Cu at (83.3, 26.1)
- added J4: PogoPinPad, CustomFootprints:PogoPinPad, F.Cu at (226.8, 117.0)
- added J4: PogoPinPad, CustomFootprints:PogoPinPad, F.Cu at (181.6, 80.8)
- added J4: PogoPinPad, CustomFootprints:PogoPinPad, F.Cu at (73.2, 153.2)
- added J4: Shield_Connector_Bottom_Right, CustomFootprints:HDR-TH_1P-V-F-1, F.Cu at (105.3, 156.7)
- added J4: Shield_Connector_Top_Left, CustomFootprints:HDR-TH_1P-V-F-1, F.Cu at (191.7, 26.1)
- added J4: PogoPinPad, CustomFootprints:PogoPinPad, F.Cu at (181.6, 44.6)
- added J4: PogoPinPad, CustomFootprints:PogoPinPad, F.Cu at (73.2, 44.6)
- added J4: Shield_Connector_Bottom_Right, CustomFootprints:HDR-TH_1P-V-F-1, F.Cu at (213.7, 156.7)
- added J4: Shield_Connector_Top_Left, CustomFootprints:HDR-TH_1P-V-F-1, F.Cu at (191.7, 98.5)
- added J4: PogoPinPad, CustomFootprints:PogoPinPad, F.Cu at (127.4, 153.2)
- added J4: Shield_Connector_Top_Left, CustomFootprints:HDR-TH_1P-V-F-1, F.Cu at (137.5, 134.7)
- added J4: Shield_Connector_Bottom_Right, CustomFootprints:HDR-TH_1P-V-F-1, F.Cu at (213.7, 84.3)
- added J4: Shield_Connector_Bottom_Right, CustomFootprints:HDR-TH_1P-V-F-1, F.Cu at (159.5, 48.1)
- added J4: PogoPinPad, CustomFootprints:PogoPinPad, F.Cu at (118.4, 117.0)
- added J4: Shield_Connector_Bottom_Right, CustomFootprints:HDR-TH_1P-V-F-1, F.Cu at (105.3, 84.3)
- added J4: PogoPinPad, CustomFootprints:PogoPinPad, F.Cu at (172.6, 80.8)
- added J4: PogoPinPad, CustomFootprints:PogoPinPad, F.Cu at (127.4, 117.0)
- added J4: PogoPinPad, CustomFootprints:PogoPinPad, F.Cu at (118.4, 44.6)
- added J4: PogoPinPad, CustomFootprints:PogoPinPad, F.Cu at (226.8, 44.6)
- added J4: PogoPinPad, CustomFootprints:PogoPinPad, F.Cu at (181.6, 117.0)
- added J4: PogoPinPad, CustomFootprints:PogoPinPad, F.Cu at (127.4, 80.8)
- added J5: Shield_Connector_Bottom_Left, CustomFootprints:HDR-TH_1P-V-F-1, F.Cu at (83.3, 48.1)
- added J5: Shield_Connector_Bottom_Left, CustomFootprints:HDR-TH_1P-V-F-1, F.Cu at (83.3, 120.5)
- added J5: Shield_Connector_Bottom_Left, CustomFootprints:HDR-TH_1P-V-F-1, F.Cu at (191.7, 120.5)
- added J5: Shield_Connector_Bottom_Left, CustomFootprints:HDR-TH_1P-V-F-1, F.Cu at (137.5, 84.3)
- added J5: Shield_Connector_Bottom_Left, CustomFootprints:HDR-TH_1P-V-F-1, F.Cu at (137.5, 156.7)
- added J5: Shield_Connector_Bottom_Left, CustomFootprints:HDR-TH_1P-V-F-1, F.Cu at (191.7, 48.1)
- added LED1: SK6812MINI-HS, CustomFootprints:LED-SK6812MINI-HS, F.Cu at (94.3, 103.7)
- added LED1: SK6812MINI-HS, CustomFootprints:LED-SK6812MINI-HS, F.Cu at (148.5, 67.5)
- added LED1: SK6812MINI-HS, CustomFootprints:LED-SK6812MINI-HS, F.Cu at (148.5, 139.9)
- added LED1: SK6812MINI-HS, CustomFootprints:LED-SK6812MINI-HS, F.Cu at (202.7, 31.3)
- added LED1: SK6812MINI-HS, CustomFootprints:LED-SK6812MINI-HS, F.Cu at (94.3, 31.3)
- added LED1: SK6812MINI-HS, CustomFootprints:LED-SK6812MINI-HS, F.Cu at (202.7, 103.7)
- added LED2: SK6812MINI-HS, CustomFootprints:LED-SK6812MINI-HS, F.Cu at (208.1, 37.1)
- added LED2: SK6812MINI-HS, CustomFootprints:LED-SK6812MINI-HS, F.Cu at (153.9, 145.7)
- added LED2: SK6812MINI-HS, CustomFootprints:LED-SK6812MINI-HS, F.Cu at (99.7, 109.5)
- added LED2: SK6812MINI-HS, CustomFootprints:LED-SK6812MINI-HS, F.Cu at (153.9, 73.3)
- added LED2: SK6812MINI-HS, CustomFootprints:LED-SK6812MINI-HS, F.Cu at (208.1, 109.5)
- added LED2: SK6812MINI-HS, CustomFootprints:LED-SK6812MINI-HS, F.Cu at (99.7, 37.1)
- added LED3: SK6812MINI-HS, CustomFootprints:LED-SK6812MINI-HS, F.Cu at (94.3, 42.9)
- added LED3: SK6812MINI-HS, CustomFootprints:LED-SK6812MINI-HS, F.Cu at (202.7, 42.9)
- added LED3: SK6812MINI-HS, CustomFootprints:LED-SK6812MINI-HS, F.Cu at (202.7, 115.3)
- added LED3: SK6812MINI-HS, CustomFootprints:LED-SK6812MINI-HS, F.Cu at (148.5, 151.5)
- added LED3: SK6812MINI-HS, CustomFootprints:LED-SK6812MINI-HS, F.Cu at (148.5, 79.1)
- added LED3: SK6812MINI-HS, CustomFootprints:LED-SK6812MINI-HS, F.Cu at (94.3, 115.3)
- added LED4: SK6812MINI-HS, CustomFootprints:LED-SK6812MINI-HS, F.Cu at (197.3, 37.1)
- added LED4: SK6812MINI-HS, CustomFootprints:LED-SK6812MINI-HS, F.Cu at (197.3, 109.5)
- added LED4: SK6812MINI-HS, CustomFootprints:LED-SK6812MINI-HS, F.Cu at (88.9, 37.1)
- added LED4: SK6812MINI-HS, CustomFootprints:LED-SK6812MINI-HS, F.Cu at (143.1, 145.7)
- added LED4: SK6812MINI-HS, CustomFootprints:LED-SK6812MINI-HS, F.Cu at (88.9, 109.5)
- added LED4: SK6812MINI-HS, CustomFootprints:LED-SK6812MINI-HS, F.Cu at (143.1, 73.3)
- added R1: 10k, Resistor_SMD:R_0402_1005Metric, F.Cu at (198.4, 30.6)
- added R1: 10k, Resistor_SMD:R_0402_1005Metric, F.Cu at (144.2, 66.8)
- added R1: 10k, Resistor_SMD:R_0402_1005Metric, F.Cu at (198.4, 103.0)
- added R1: 10k, Resistor_SMD:R_0402_1005Metric, F.Cu at (144.2, 139.2)
- added R1: 10k, Resistor_SMD:R_0402_1005Metric, F.Cu at (90.0, 103.0)
- added R1: 10k, Resistor_SMD:R_0402_1005Metric, F.Cu at (90.0, 30.6)
- added R2: 10k, Resistor_SMD:R_0402_1005Metric, F.Cu at (207.0, 103.0)
- added R2: 10k, Resistor_SMD:R_0402_1005Metric, F.Cu at (152.8, 66.8)
- added R2: 10k, Resistor_SMD:R_0402_1005Metric, F.Cu at (207.0, 30.6)
- added R2: 10k, Resistor_SMD:R_0402_1005Metric, F.Cu at (98.6, 103.0)
- added R2: 10k, Resistor_SMD:R_0402_1005Metric, F.Cu at (98.6, 30.6)
- added R2: 10k, Resistor_SMD:R_0402_1005Metric, F.Cu at (152.8, 139.2)
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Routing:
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- added copper zone on F.Cu, net Board_1-+5V
- added copper zone on B.Cu, net Board_1-GND
- added copper zone on F.Cu, net Board_11-+5V
- added copper zone on B.Cu, net Board_11-GND
- added copper zone on F.Cu, net Board_3-+5V
- added copper zone on B.Cu, net Board_3-GND
- added copper zone on F.Cu, net Board_4-+5V
- added copper zone on B.Cu, net Board_4-GND
- added copper zone on F.Cu, net Board_6-+5V
- added copper zone on B.Cu, net Board_6-GND
- added copper zone on F.Cu, net Board_9-+5V
- added copper zone on B.Cu, net Board_9-GND
- removed copper zone on B.Cu, net (none)
- removed copper zone on F.Cu, net (none)
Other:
- outline, holes or cut-outs redrawn
